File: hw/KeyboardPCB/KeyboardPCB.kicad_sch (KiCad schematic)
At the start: 176 parts, among them IC1 TPS2113ADRBR, IC2 BGM220PC22HNA2R, J1 USB_B_Micro, J2 Conn_01x07_Pin, J3 Conn_01x06_Pin, J4 Conn_02x05_Odd_Even, J5 BATT_POS, J6 BATT_NEG, K1 KEYSW, K10 KEYSW, K11 KEYSW, K12 KEYSW, K13 KEYSW, K14 KEYSW, K15 KEYSW, K16 KEYSW, K17 KEYSW, K18 KEYSW, K19 KEYSW, K2 KEYSW, K20 KEYSW, K21 KEYSW, K22 KEYSW, K23 KEYSW, K24 KEYSW, K25 KEYSW, K26 KEYSW, K27 KEYSW, K28 KEYSW, K29 KEYSW, K3 KEYSW, K30 KEYSW, K31 KEYSW, K32 KEYSW, K33 KEYSW, K34 KEYSW, K35 KEYSW, K36 KEYSW, K37 KEYSW, K38 KEYSW, K39 KEYSW, K4 KEYSW, K40 KEYSW, K41 KEYSW, K42 KEYSW, K43 KEYSW, K44 KEYSW, K45 KEYSW, K46 KEYSW, K47 KEYSW, K48 KEYSW, K49 KEYSW, K5 KEYSW, K50 KEYSW, K51 KEYSW, K52 KEYSW, K53 KEYSW, K54 KEYSW, K55 KEYSW, K56 KEYSW, K57 KEYSW, K58 KEYSW, K59 KEYSW, K6 KEYSW, K60 KEYSW, K61 KEYSW, K62 KEYSW, K7 KEYSW, K8 KEYSW, K9 KEYSW, SW2 BAT_SWITCH, U1 TM4C123GH6PMI7, U2 TPS73633DBV, U3 Adafruit ST7735R, X2 16MHz

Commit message: Slight tweaks
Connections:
- net GND: no longer U1.61 (PD0)
- net EM4_WAKEUP: now reaches IC2.22 (PC00)
- net EM4_WAKEUP: now also U1.61 (PD0)
- no-connect marks 20 -> 19
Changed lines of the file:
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@@
   (no_connect (at 200.66 127))
   (no_connect (at 323.85 236.22))
-  (no_connect (at 356.87 246.38))
   (no_connect (at 147.32 306.07))
   (no_connect (at 128.27 241.3))
@@
     (stroke (width 0) (type default))
   )
-  (wire (pts (xy 170.18 118.11) (xy 167.64 118.11))
-    (stroke (width 0) (type default))
-  )
   (wire (pts (xy 321.31 139.7) (xy 321.31 157.48))
     (stroke (width 0) (type default))
@@
     (stroke (width 0) (type default))
   )
-  (wire (pts (xy 167.64 118.11) (xy 167.64 119.38))
-    (stroke (width 0) (type default))
-  )
   (wire (pts (xy 497.84 93.98) (xy 519.43 93.98))
     (stroke (width 0) (type default))
@@
     (effects (font (size 1.27 1.27)) (justify left bottom))
   )
+  (label "EM4_WAKEUP" (at 167.64 119.38 0) (fields_autoplaced)
+    (effects (font (size 1.27 1.27)) (justify left bottom))
+  )
   (label "col10" (at 494.03 80.01 0) (fields_autoplaced)
     (effects (font (size 1.27 1.27)) (justify left bottom))
@@
     (effects (font (size 1.27 1.27)) (justify right bottom))
   )
+  (label "EM4_WAKEUP" (at 356.87 246.38 0) (fields_autoplaced)
+    (effects (font (size 1.27 1.27)) (justify left bottom))
+  )
   (label "BGM_SWDIO" (at 323.85 254 180) (fields_autoplaced)
     (effects (font (size 1.27 1.27)) (justify right bottom))
@@
         )
       )
-    )
-  )
-  (symbol (lib_id "power:GND") (at 170.18 118.11 90) (unit 1)
-    (in_bom yes) (on_board yes) (dnp no) (fields_autoplaced)
-    (property "Reference" "#PWR017" (at 176.53 118.11 0)
-      (effects (font (size 1.27 1.27)) hide)
-    )
-    (property "Value" "GND" (at 173.99 118.11 90)
-      (effects (font (size 1.27 1.27)) (justify right))
-    )
-    (property "Footprint" "" (at 170.18 118.11 0)
-      (effects (font (size 1.27 1.27)) hide)
-    )
-    (property "Datasheet" "" (at 170.18 118.11 0)
-      (effects (font (size 1.27 1.27)) hide)
-    )
-    (pin "1")
-    (instances
-      (project "KeyboardPCB"
-        (path "/2d193c8d-36cd-4337-adc1-05f8d95a4b88"
-          (reference "#PWR017") (unit 1)
-        )
-      )

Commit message: :)
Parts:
- removed R3, R4: 22, Resistor_SMD:R_0402_1005Metric, symbol Device:R
- removed TP1: USB_DM, TestPoint:TestPoint_Pad_2.5x2.5mm, symbol Connector:TestPoint
- removed TP2: USB_DP, TestPoint:TestPoint_Pad_2.5x2.5mm, symbol Connector:TestPoint
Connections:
- net LED_control is gone; now on net GND: U1.47 (PB2_I2C0SCL), U1.48 (PB3_I2C0SDA)
- net BGM220P_DEBUG_RX: now also J3.2 (Pin_2); no longer J3.1 (Pin_1)
- net GND: now also U1.53 (PD6)
- net col0: now also U1.14 (PC6); no longer U1.58 (PB4)
- net col1: now also U1.13 (PC7); no longer U1.57 (PB5)
- net col10: now also U1.60 (PE5); no longer U1.14 (PC6)
- net col11: now also U1.59 (PE4); no longer U1.13 (PC7)
- net col12: now also U1.58 (PB4); no longer U1.53 (PD6)
- net col13: now also U1.57 (PB5); no longer U1.10 (PD7)
- net col2: now also U1.10 (PD7); no longer U1.1 (PB6)
- net col3: now also U1.9 (PE0); no longer U1.4 (PB7)
- net col4: now also U1.8 (PE1); no longer U1.9 (PE0)
- net col5: now also U1.7 (PE2); no longer U1.8 (PE1)
- net col6: now also U1.6 (PE3); no longer U1.7 (PE2)
- net col7: now also U1.5 (PF4); no longer U1.6 (PE3)
- net col8: now also U1.4 (PB7); no longer U1.59 (PE4)
- net col9: now also U1.1 (PB6); no longer U1.60 (PE5)
- net row0: now also U1.31 (PF3); no longer U1.28 (PF0)
- net row1: now also U1.30 (PF2); no longer U1.29 (PF1)
- net row2: now also U1.29 (PF1); no longer U1.30 (PF2)
- net row3: now also U1.28 (PF0); no longer U1.31 (PF3)
- net row4: no longer U1.5 (PF4)
- net USB_D-: now reaches U1.43 (PD4)
- net USB_D-: now also J1.2 (D-)
- net USB_D+: now reaches U1.44 (PD5)
- net USB_D+: now also J1.3 (D+)
- net BMG220P_DEBUG_TX renamed BGM220P_DEBUG_TX
- net BGM220P_DEBUG_TX: now also J3.1 (Pin_1); no longer J3.2 (Pin_2)

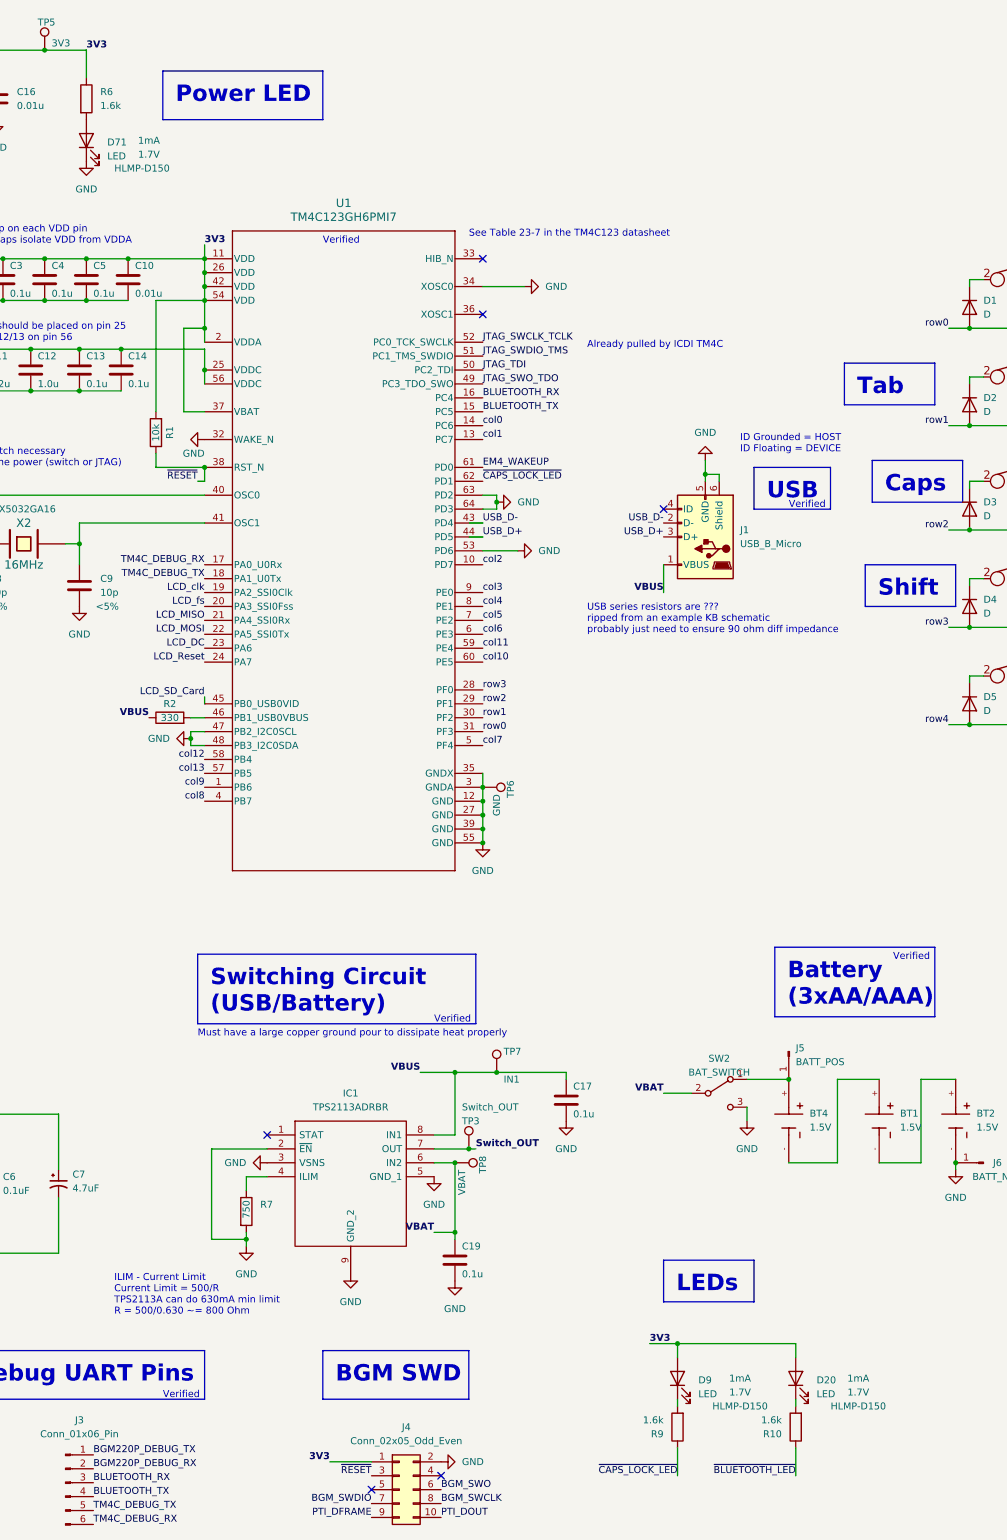
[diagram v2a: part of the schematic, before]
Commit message: Updated BoM to include LEDs and M2x4 mounting screws.
Length of screws can be updated depending on the thickness of the PCB

Also updated resistor values based on forward voltage of SMD LEDs
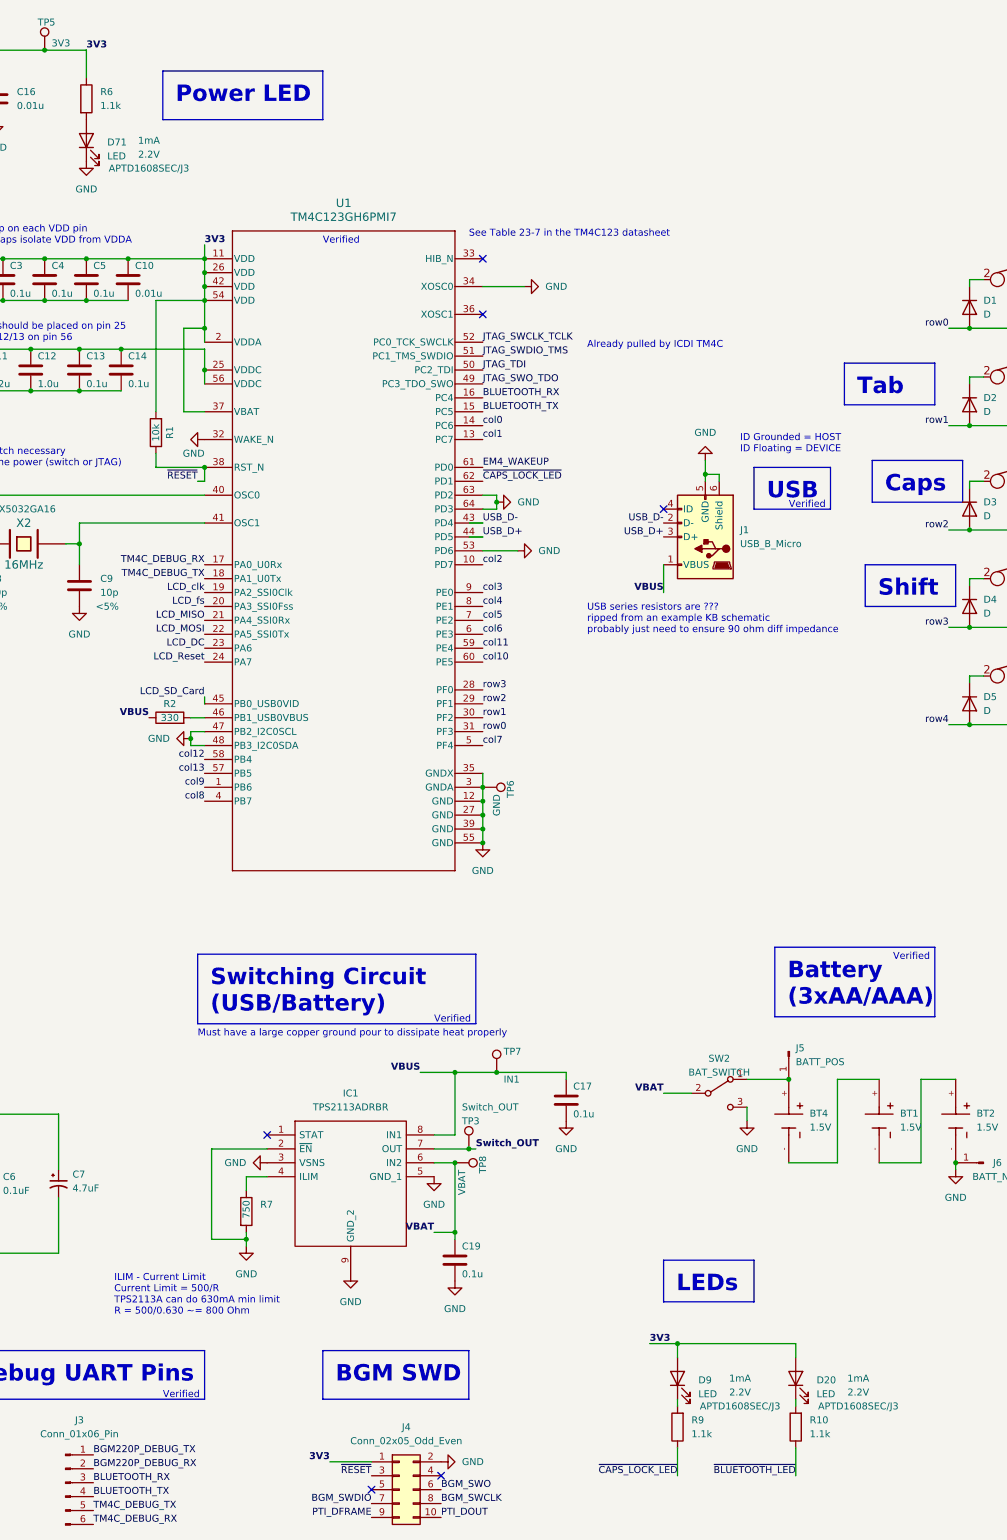
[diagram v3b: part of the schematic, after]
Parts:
- D20, D71, D9: footprint LED_THT:LED_D5.0mm -> LED_SMD:LED_0603_1608Metric_Pad1.05x0.95mm_HandSolder; Part HLMP-D150 -> APTD1608SEC/J3; Vf 1.7V -> 2.2V
- R10, R6, R9: value 1.6k -> 1.1k
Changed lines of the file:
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@@
   (symbol (lib_id "Device:R") (at 203.2 294.64 180) (unit 1)
     (in_bom yes) (on_board yes) (dnp no) (fields_autoplaced)
-    (property "Reference" "R9" (at 200.66 295.91 0)
-      (effects (font (size 1.27 1.27)) (justify left))
-    )
-    (property "Value" "1.6k" (at 200.66 293.37 0)
-      (effects (font (size 1.27 1.27)) (justify left))
+    (property "Reference" "R9" (at 205.74 293.37 0)
+      (effects (font (size 1.27 1.27)) (justify right))
+    )
+    (property "Value" "1.1k" (at 205.74 295.91 0)
+      (effects (font (size 1.27 1.27)) (justify right))
     )
     (property "Footprint" "Resistor_SMD:R_0402_1005Metric" (at 204.978 294.64 90)
@@
       (effects (font (size 1.27 1.27)) (justify left))
     )
-    (property "Value" "1.6k" (at 97.79 53.34 0)
+    (property "Value" "1.1k" (at 97.79 53.34 0)
       (effects (font (size 1.27 1.27)) (justify left))
     )
@@
       (effects (font (size 1.27 1.27)) (justify right))
     )
-    (property "Footprint" "LED_THT:LED_D5.0mm" (at 95.25 59.69 0)
+    (property "Footprint" "LED_SMD:LED_0603_1608Metric_Pad1.05x0.95mm_HandSolder" (at 95.25 59.69 0)
       (effects (font (size 1.27 1.27)) hide)
     )
@@
       (effects (font (size 1.27 1.27)) hide)
     )
-    (property "Part" "HLMP-D150" (at 105.41 64.77 90)
+    (property "Part" "APTD1608SEC/J3" (at 106.68 64.77 90)
       (effects (font (size 1.27 1.27)))
     )
-    (property "Vf" "1.7V" (at 106.68 62.23 90)
+    (property "Vf" "2.2V" (at 106.68 62.23 90)
       (effects (font (size 1.27 1.27)))
     )
@@
       (effects (font (size 1.27 1.27)) (justify right))
     )
-    (property "Footprint" "LED_THT:LED_D5.0mm" (at 203.2 285.75 0)
+    (property "Footprint" "LED_SMD:LED_0603_1608Metric_Pad1.05x0.95mm_HandSolder" (at 203.2 285.75 0)
       (effects (font (size 1.27 1.27)) hide)
     )
@@
       (effects (font (size 1.27 1.27)) hide)
     )
-    (property "Part" "HLMP-D150" (at 214.63 290.83 90)
+    (property "Part" "APTD1608SEC/J3" (at 214.63 290.83 90)
       (effects (font (size 1.27 1.27)))
     )
-    (property "Vf" "1.7V" (at 214.63 288.29 90)
+    (property "Vf" "2.2V" (at 214.63 288.29 90)
       (effects (font (size 1.27 1.27)))
     )
@@
       (effects (font (size 1.27 1.27)) (justify right))
     )
-    (property "Footprint" "LED_THT:LED_D5.0mm" (at 224.79 285.75 0)
+    (property "Footprint" "LED_SMD:LED_0603_1608Metric_Pad1.05x0.95mm_HandSolder" (at 224.79 285.75 0)
       (effects (font (size 1.27 1.27)) hide)
     )
@@
       (effects (font (size 1.27 1.27)) hide)
     )
-    (property "Part" "HLMP-D150" (at 236.22 290.83 90)
+    (property "Part" "APTD1608SEC/J3" (at 236.22 290.83 90)
       (effects (font (size 1.27 1.27)))
     )
-    (property "Vf" "1.7V" (at 236.22 288.29 90)
+    (property "Vf" "2.2V" (at 236.22 288.29 90)
       (effects (font (size 1.27 1.27)))
     )
@@
   (symbol (lib_id "Device:R") (at 224.79 294.64 180) (unit 1)
     (in_bom yes) (on_board yes) (dnp no) (fields_autoplaced)
-    (property "Reference" "R10" (at 222.25 295.91 0)
-      (effects (font (size 1.27 1.27)) (justify left))
-    )
-    (property "Value" "1.6k" (at 222.25 293.37 0)
-      (effects (font (size 1.27 1.27)) (justify left))
+    (property "Reference" "R10" (at 227.33 293.37 0)
+      (effects (font (size 1.27 1.27)) (justify right))
+    )
+    (property "Value" "1.1k" (at 227.33 295.91 0)
+      (effects (font (size 1.27 1.27)) (justify right))
     )
     (property "Footprint" "Resistor_SMD:R_0402_1005Metric" (at 226.568 294.64 90)

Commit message: PCB done!
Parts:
- added R3, R4: 22, Resistor_SMD:R_0402_1005Metric, symbol Device:R
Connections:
- net USB_D+: no longer names the net of U1.44 (PD5)
- net USB_D+: now also R4.1; no longer J1.3 (D+)
- net USB_D-: no longer names the net of U1.43 (PD4)
- net USB_D-: now also R3.1; no longer J1.2 (D-)
- new net: J1.2 (D-), R3.2
- new net: J1.3 (D+), R4.2
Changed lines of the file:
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@@
   (junction (at 411.48 93.98) (diameter 0) (color 0 0 0 0)
   )
+  (junction (at 167.64 132.08) (diameter 0) (color 0 0 0 0)
+  )
   (junction (at 472.44 102.87) (diameter 0) (color 0 0 0 0)
   )
@@
   (junction (at 407.67 121.92) (diameter 0) (color 0 0 0 0)
   )
+  (junction (at 167.64 129.54) (diameter 0) (color 0 0 0 0)
+  )
   (junction (at 364.49 85.09) (diameter 0) (color 0 0 0 0)
   )
@@
     (stroke (width 0) (type default))
   )
+  (wire (pts (xy 189.23 129.54) (xy 200.66 129.54))
+    (stroke (width 0) (type default))
+  )
   (wire (pts (xy 476.25 121.92) (xy 478.79 121.92))
     (stroke (width 0) (type default))
@@
     (stroke (width 0) (type default))
   )
+  (wire (pts (xy 167.64 132.08) (xy 181.61 132.08))
+    (stroke (width 0) (type default))
+  )
   (wire (pts (xy 256.54 121.92) (xy 259.08 121.92))
     (stroke (width 0) (type default))
@@
     (stroke (width 0) (type default))
   )
+  (wire (pts (xy 189.23 132.08) (xy 200.66 132.08))
+    (stroke (width 0) (type default))
+  )
   (wire (pts (xy 497.84 93.98) (xy 519.43 93.98))
     (stroke (width 0) (type default))
@@
     (stroke (width 0) (type default))
   )
+  (wire (pts (xy 167.64 129.54) (xy 181.61 129.54))
+    (stroke (width 0) (type default))
+  )
   (wire (pts (xy 90.17 252.73) (xy 90.17 262.89))
     (stroke (width 0) (type default))
@@
     (effects (font (size 1.27 1.27)) (justify right bottom))
   )
-  (label "USB_D-" (at 167.64 129.54 0) (fields_autoplaced)
-    (effects (font (size 1.27 1.27)) (justify left bottom))
-  )
   (label "PTI_DOUT" (at 356.87 256.54 0) (fields_autoplaced)
     (effects (font (size 1.27 1.27)) (justify left bottom))
@@
     (effects (font (size 1.27 1.27)) (justify left bottom))
   )
-  (label "USB_D+" (at 200.66 132.08 180) (fields_autoplaced)
-    (effects (font (size 1.27 1.27)) (justify right bottom))
-  )
   (label "BLUETOOTH_TX" (at 96.52 307.34 0) (fields_autoplaced)
     (effects (font (size 1.27 1.27)) (justify left bottom))
@@
     (effects (font (size 1.27 1.27)) (justify left bottom))
   )
-  (label "USB_D+" (at 167.64 132.08 0) (fields_autoplaced)
-    (effects (font (size 1.27 1.27)) (justify left bottom))
-  )
   (label "EM4_WAKEUP" (at 167.64 119.38 0) (fields_autoplaced)
     (effects (font (size 1.27 1.27)) (justify left bottom))
@@
     (effects (font (size 1.27 1.27)) (justify left bottom))
   )
-  (label "USB_D-" (at 200.66 129.54 180) (fields_autoplaced)
-    (effects (font (size 1.27 1.27)) (justify right bottom))
-  )
   (label "JTAG_SWDIO_TMS" (at 27.94 302.26 0) (fields_autoplaced)
     (effects (font (size 1.27 1.27)) (justify left bottom))
@@
     )
   )
+  (symbol (lib_id "Device:R") (at 185.42 129.54 90) (unit 1)
+    (in_bom yes) (on_board yes) (dnp no)
+    (property "Reference" "R3" (at 185.42 127 90)
+      (effects (font (size 1.27 1.27)))
+    )
+    (property "Value" "22" (at 185.42 129.54 90)
+      (effects (font (size 1.27 1.27)))
+    )
+    (property "Footprint" "Resistor_SMD:R_0402_1005Metric" (at 185.42 131.318 90)
+      (effects (font (size 1.27 1.27)) hide)
+    )
+    (property "Datasheet" "~" (at 185.42 129.54 0)
+      (effects (font (size 1.27 1.27)) hide)
+    )
+    (pin "1")
+    (pin "2")
+    (instances
+      (project "KeyboardPCB"
+        (path "/2d193c8d-36cd-4337-adc1-05f8d95a4b88"
+          (reference "R3") (unit 1)
+        )
+      )
+    )
+  )
   (symbol (lib_id "keyboard_parts:KEYSW") (at 335.28 121.92 0) (unit 1)
     (in_bom yes) (on_board yes) (dnp no) (fields_autoplaced)
@@
         )
       )
+    )
+  )
+  (symbol (lib_id "Device:R") (at 185.42 132.08 90) (unit 1)
+    (in_bom yes) (on_board yes) (dnp no)
+    (property "Reference" "R4" (at 185.42 134.62 90)
+      (effects (font (size 1.27 1.27)))
+    )
+    (property "Value" "22" (at 185.42 132.08 90)
+      (effects (font (size 1.27 1.27)))
+    )
+    (property "Footprint" "Resistor_SMD:R_0402_1005Metric" (at 185.42 133.858 90)
+      (effects (font (size 1.27 1.27)) hide)
+    )
+    (property "Datasheet" "~" (at 185.42 132.08 0)
+      (effects (font (size 1.27 1.27)) hide)
+    )
+    (pin "1")
+    (pin "2")
+    (instances
+      (project "KeyboardPCB"
+        (path "/2d193c8d-36cd-4337-adc1-05f8d95a4b88"
+          (reference "R4") (unit 1)
+        )
+      )

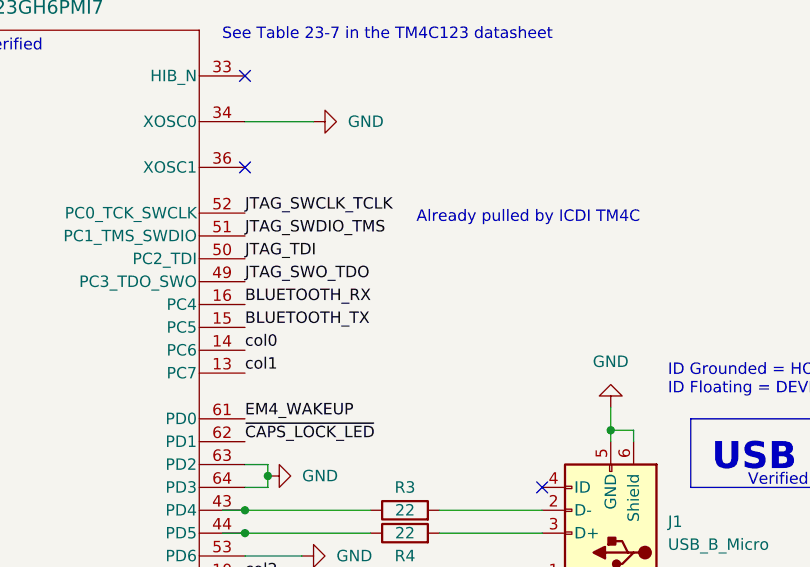
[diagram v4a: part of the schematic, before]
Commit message: Routed row4 to JTAG_TDO
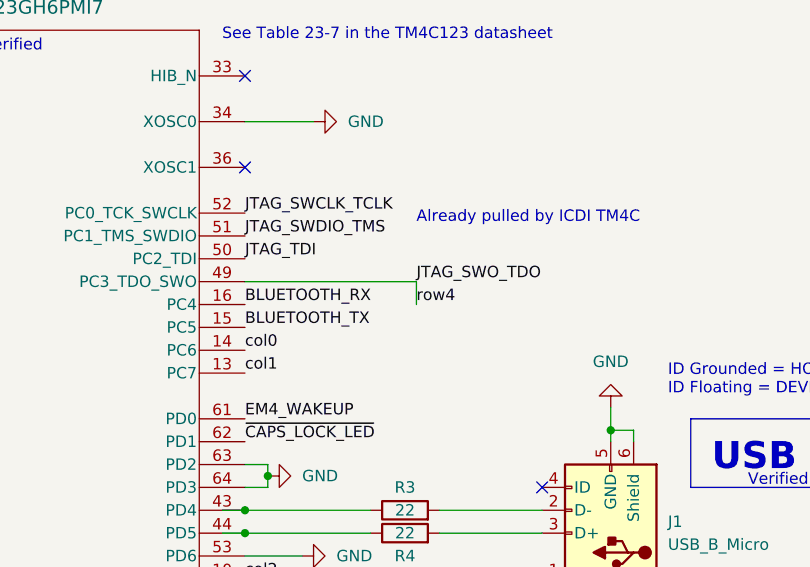
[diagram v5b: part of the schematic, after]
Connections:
- net row4 is gone; now on net JTAG_SWO_TDO: D10.2 (A), D15.2 (A), D30.2 (A), D5.2 (A), D50.2 (A), D55.2 (A), D60.2 (A), D65.2 (A)
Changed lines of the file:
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@@
+    (stroke (width 0) (type default))
+  )
+  (wire (pts (xy 186.69 104.14) (xy 186.69 106.68))
     (stroke (width 0) (type default))
   )
@@
   )
   (wire (pts (xy 494.03 102.87) (xy 494.03 121.92))
+    (stroke (width 0) (type default))
+  )
+  (wire (pts (xy 186.69 104.14) (xy 167.64 104.14))
     (stroke (width 0) (type default))
   )
@@
     (effects (font (size 1.27 1.27) (thickness 0.254) bold) (justify right bottom))
   )
+  (label "row4" (at 186.69 106.68 0) (fields_autoplaced)
+    (effects (font (size 1.27 1.27)) (justify left bottom))
+  )
   (label "col8" (at 450.85 80.01 0) (fields_autoplaced)
     (effects (font (size 1.27 1.27)) (justify left bottom))
@@
     (effects (font (size 1.27 1.27)) (justify left bottom))
   )
-  (label "JTAG_SWO_TDO" (at 167.64 104.14 0) (fields_autoplaced)
-    (effects (font (size 1.27 1.27)) (justify left bottom))
-  )
+  (label "JTAG_SWO_TDO" (at 186.69 104.14 0) (fields_autoplaced)
+    (effects (font (size 1.27 1.27)) (justify left bottom))
+  )
